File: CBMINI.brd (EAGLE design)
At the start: 100 x 60 mm, 47 parts, among them J1 USB_B_PTH, SW1 SWITCH-DPDT3, U1 MCP2551, X1 INPUT, X2 OUTPUT

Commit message: Changed CAN crystal to 16MHz for compatibility with Arduino CAN shields
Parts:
- XTL2: value 8MHz -> 16MHz
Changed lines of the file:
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@@
 <attribute name="VALUE" x="48.984" y="26.5348" size="1.016" layer="27" font="vector"/>
 </element>
-<element name="XTL2" library="freetronics-jon" package="CRYSTAL-SMD-3X2" value="8MHz" x="51" y="31" smashed="yes" rot="R180">
+<element name="XTL2" library="freetronics-jon" package="CRYSTAL-SMD-3X2" value="16MHz" x="51" y="31" smashed="yes" rot="R180">
 <attribute name="NAME" x="52.54" y="29.395" size="0.4064" layer="25" rot="R180"/>
 <attribute name="VALUE" x="47.96" y="32.46" size="1.016" layer="27"/>

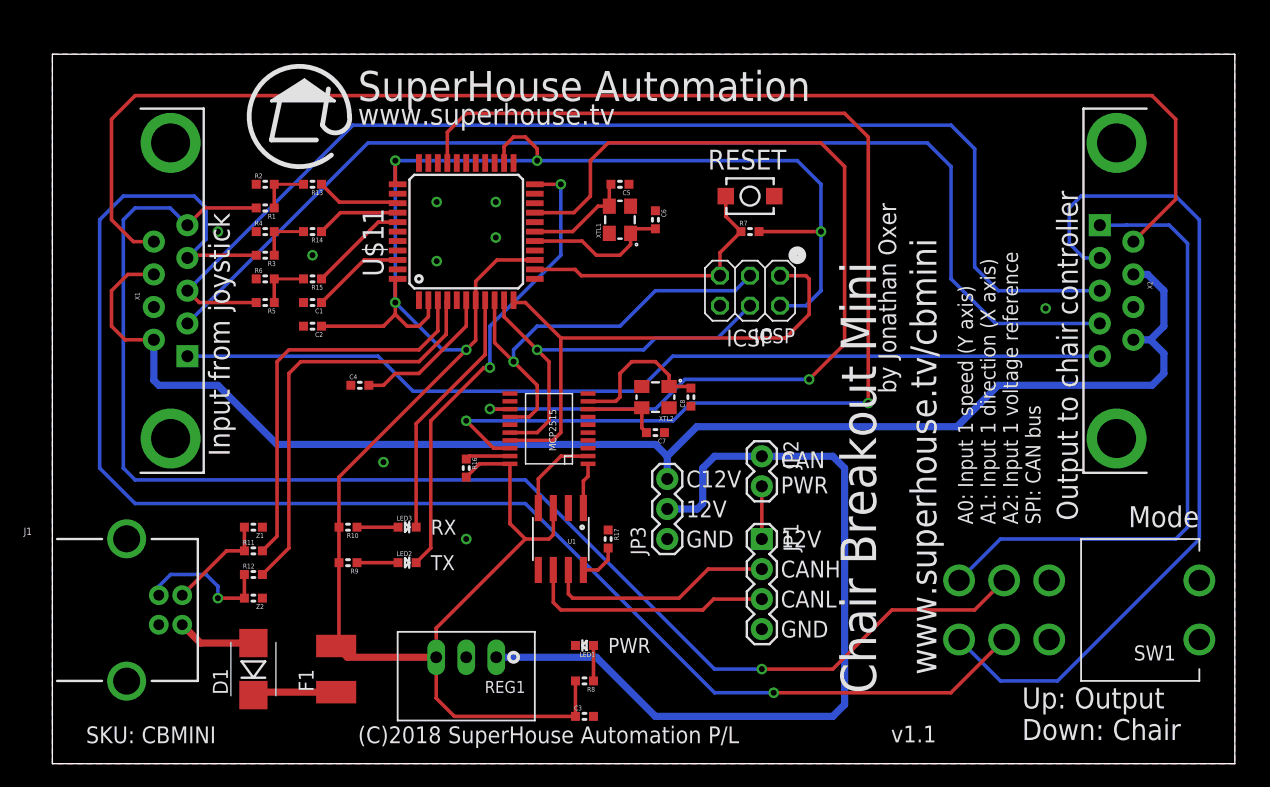
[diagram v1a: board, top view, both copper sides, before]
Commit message: Added extra input channels and CAN termination for v2.0 release
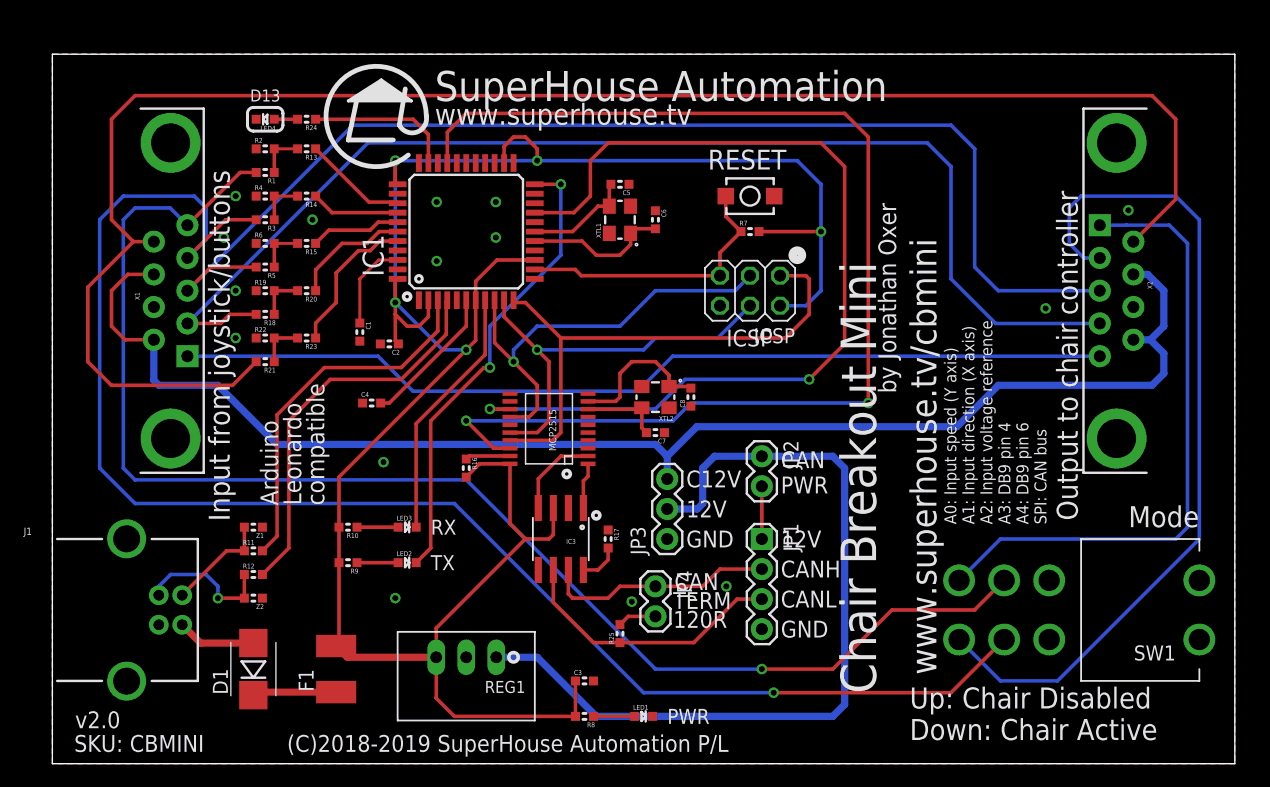
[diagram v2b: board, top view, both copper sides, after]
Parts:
- added JP4: PWR, freetronics-jon:1X02
- added LED4: GREEN, freetronics-jon:LED-0603
- added R18, R19, R21, R22: 47K 1%, freetronics-jon:0603
- added R20, R23, R24: 1K, freetronics-jon:0603
- added R25: 120R, freetronics-master-v1.1:0603
- moved LED1 7.81 mm to (50.0, 4.00), turned to 0 degrees
- moved C2 6.67 mm to (28.5, 35.5)
- moved C1 4.72 mm to (26.0, 36.5), turned to 270 degrees
- moved R13 3.04 mm to (21.5, 52.0)
- moved R14 3.04 mm to (21.5, 48.0)
- moved R15 3.04 mm to (21.5, 44.0)
- moved C3 3.00 mm to (45.0, 7.00)
- moved R1 3.00 mm to (18.0, 50.0)
- moved R2 3.00 mm to (18.0, 52.0)
- moved R3 3.00 mm to (18.0, 46.0)
- moved R4 3.00 mm to (18.0, 48.0)
- moved R5 3.00 mm to (18.0, 42.0)
- moved R6 3.00 mm to (18.0, 44.0)
- moved R8 3.00 mm to (45.0, 4.00)
- moved C4 1.80 mm to (27.0, 30.5)
- renumbered U$11 to IC1, U$4 to IC2, U1 to IC3
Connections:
- removed net N$6: X1.4, X2.4
- new net N$19: R18.1, R19.2, R20.2
- new net N$20: JP4.2, R25.2
- new net N$21: R21.1, R22.2, R23.2
- new net PIN4: R18.2, X1.4, X2.4
- new net PIN6: R21.2, X1.6, X2.6
- net A3: now also R20.1
- net A4: now also R23.1
- net CANH: now also JP4.1
- net CANL: now also R25.1
- net D13: now also R24.1
- net GND: now also LED4.C, R19.1, R22.1
- net N$1: now also LED4.A, R24.2; no longer X1.6, X2.6
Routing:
- net PIN6: track 0.00 -> 144.0 mm
- net N$1: track 116.3 -> 1.98 mm
- net PIN4: track 0.00 -> 101.5 mm
- net N$6: track 95.4 -> 0.00 mm
- net A4: track 0.00 -> 12.5 mm
- net D13: track 0.00 -> 12.5 mm
- net A3: track 0.00 -> 10.0 mm
- net 5V: track 195.6 -> 191.5 mm
- net N$21: track 0.00 -> 3.98 mm
- net N$19: track 0.00 -> 3.98 mm
- net N$20: track 0.00 -> 3.29 mm
- net RD-: track 33.8 -> 31.2 mm
- net RD+: track 35.5 -> 33.2 mm
- net CANL: track 21.0 -> 23.3 mm
- net A0: track 7.10 -> 8.84 mm
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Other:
- board text added: "(C)2018-2019 SuperHouse Automation P/L"
- board text added: "120R"
- board text added: "A0: Input speed (Y axis) A1: Input direction (X axis) A2: Input voltage reference A3: DB9 pin 4 A4: DB9 pin 6 SPI: CAN bus"
- board text added: "Arduino Leonardo compatible"
- board text added: "CAN"
- board text added: "D13"
- board text added: "Input from joystick/buttons"
- board text added: "Released under the TAPR Open Hardware License: tapr.org/OHL"
- board text added: "TERM"
- board text added: "Up: Chair Disabled Down: Chair Active"
- board text added: "v2.0"
- board text removed: "(C)2018 SuperHouse Automation P/L"
- board text removed: "A0: Input 1 speed (Y axis) A1: Input 1 direction (X axis) A2: Input 1 voltage reference SPI: CAN bus"
- board text removed: "Input from joystick"
- board text removed: "Up: Output Down: Chair"
- board text removed: "v1.1"
